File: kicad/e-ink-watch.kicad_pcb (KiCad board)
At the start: 4 copper layers, 40 x 40 mm, 42 parts, among them SW1 BTN1, SW2 BTN2, SW3 BTN3, U1 MDBT50Q-1MV2, U2 BQ25120A

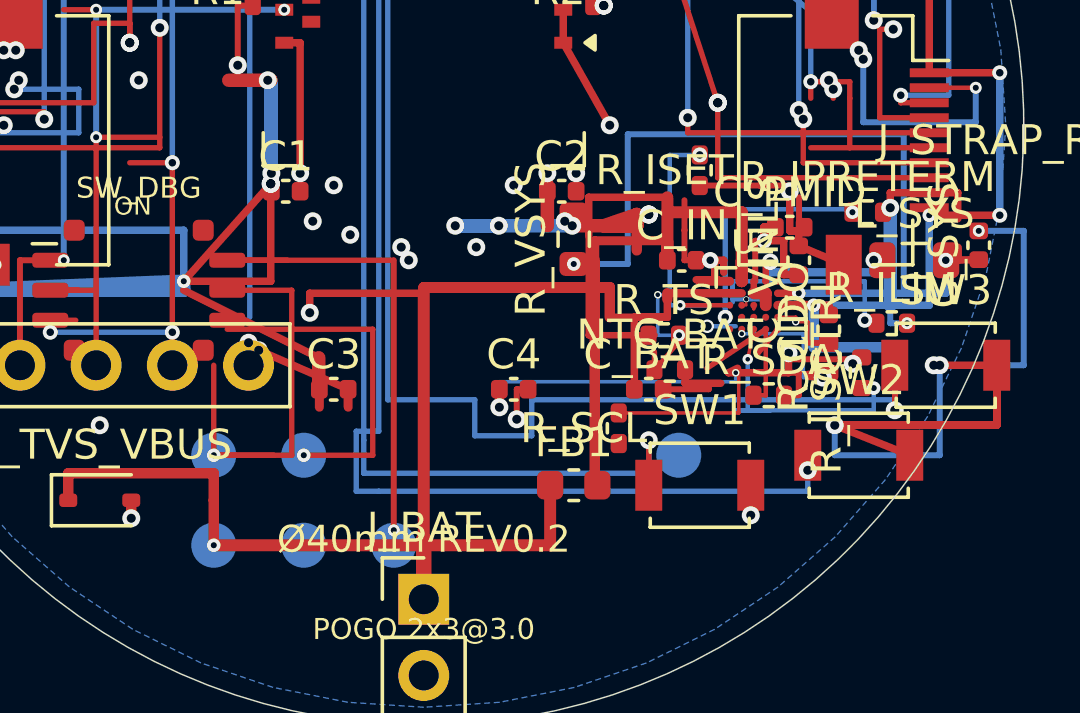
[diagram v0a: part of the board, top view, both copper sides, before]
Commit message: Pass-AT/AV: R_SCL on E5 (unc 6); VBUS jog cannot open I2C (#6)
* Pass-AL: keep the west GND via after a local In2 notch.

A 0.25/0.15 GND via on the west F end at (108.71, 108.15) joins the B.Cu pour. The In2 3V3 outline is notched with a 0.45 mm arc so the drill does not hit the plane. DRC stays shorting 0 and unconnected drops 8 to 7. South passives and U2 were not moved.

Co-authored-by: illiapliukhin <illiapliukhin@users.noreply.github.com>

* Pass-AM: record that R_SDA cannot leave x=111.4.

A larger placement search found an SCL hop under the 3V3 rail once the R_SDA vertical is gone, and a clear R_SCL site on that run. No R_SDA park has a 0.15 mm retie to E4, so the board is unchanged. Unconnected stays 7 and shorting stays 0.

Co-authored-by: illiapliukhin <illiapliukhin@users.noreply.github.com>

* Pass-AN: record that larger R_SDA moves still cannot retie 3V3.

The SCL hop at x=111.35 sits 0.015 mm from the B GND pour, so it stays unapplied. Unconnected remains 7 and shorting remains 0.

Co-authored-by: illiapliukhin <illiapliukhin@users.noreply.github.com>

* Pass-AO: record blocked PMIC_INT, TS, 3V3_DISP, and A5 stitches.

No footprint moved and no copper was added. Unconnected remains 7 and shorting remains 0.

Co-authored-by: illiapliukhin <illiapliukhin@users.noreply.github.com>

* Pass-AP: revert U2 zone move that joins SCL but raises shorting.

R_SCL onto E5 drops unc 7 to 6 and DRC then reports SWDIO_POGO to 3V3. Rigid 1-2 mm island shifts overlap. Board stays at the Pass-AL file.

Co-authored-by: illiapliukhin <illiapliukhin@users.noreply.github.com>

* Pass-AQ: revert clean U2 re-fanout; R_SCL on E5 still raises SWDIO short.

Shrinking the local 3V3 via and sliding the D5 GND via stays at shorting 0 and unc 7. Seating R_SCL on E5 drops unc to 6 and raises SWDIO_POGO↔3V3. Full revert; board stays the Pass-AL KEEP.

Co-authored-by: illiapliukhin <illiapliukhin@users.noreply.github.com>

* Pass-AR: revert SW_DBG move; pad 6 still overlaps the 3V3 dia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
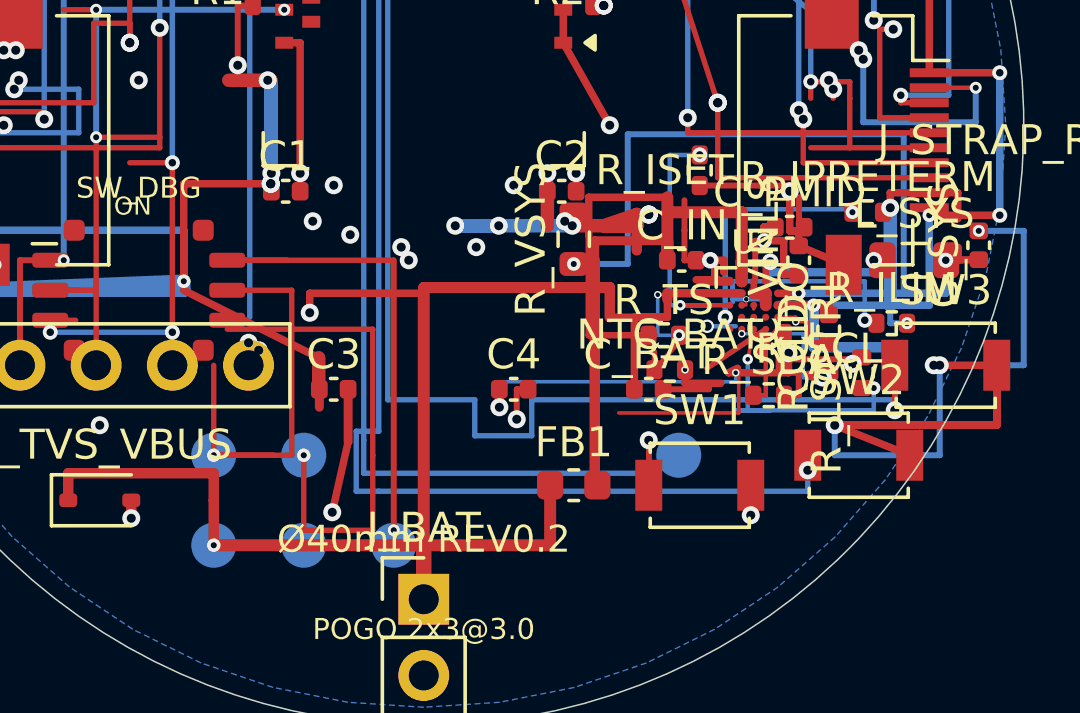
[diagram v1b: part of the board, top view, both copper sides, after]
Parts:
- moved R_SCL 6.11 mm to (112.0, 107.5), turned to 270 degrees
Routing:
- net nRESET_POGO: track 11.3 -> 16.3 mm
- net 3V3: track 114.8 -> 111.2 mm
- net GND: track 140.9 -> 141.2 mm, vias 44 -> 46
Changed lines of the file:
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@@
 	(footprint "Resistor_SMD:R_0402_1005Metric"
 		(layer "F.Cu")
-		(at 106.5 110.1 90)
+		(at 112 107.45 270)
 		(descr "Resistor SMD 0402 (1005 Metric), square (rectangular) end terminal, IPC-7351 nominal, (Body size source: IPC-SM-782 page 72, https://www.pcb-3d.com/wordpress/wp-content/uploads/ipc-sm-782a_amendment_1_and_2.pdf), generated with kicad-footprint-generator")
 		(tags "resistor")
@@
 	(segment
 		(start 97.48 108.8)
-		(end 97.48 109.399999)
+		(end 97.48 110.55)
 		(width 0.3)
 		(layer "F.Cu")
@@
 	)
 	(segment
-		(start 98.3 111)
-		(end 96 111)
-		(width 0.18)
-		(layer "F.Cu")
-		(net 25)
-	)
-	(segment
 		(start 98.3 106.8)
 		(end 98.3 111)
@@
 	)
 	(segment
-		(start 97.48 108.8)
-		(end 94.5 107.5)
-		(width 0.25)
-		(layer "F.Cu")
-		(net 1)
-	)
-	(segment
 		(start 85.0 96.5)
 		(end 85.0 94.5)
@@
 	(segment
 		(start 94.9 101.95)
-		(end 92.0 105.2)
+		(end 92.0 101.95)
 		(width 0.25)
 		(layer "F.Cu")
@@
 	)
 	(segment
-		(start 94.9 101.95)
-		(end 94.9 105.2)
+		(start 92.0 101.95)
+		(end 92.0 105.2)
 		(width 0.25)
 		(layer "F.Cu")
@@
 	)
 	(segment
-		(start 94.9 105.2)
+		(start 92.0 104.4)
 		(end 92.0 105.2)
 		(width 0.25)
@@
 	)
 	(via
+		(at 108.71 108.15)
+		(size 0.25)
+		(drill 0.15)
+		(layers "F.Cu" "B.Cu")
+		(net 1)
+	)
+	(segment
+		(start 97.48 110.55)
+		(end 96.95 112.9)
+		(width 0.25)
+		(layer "F.Cu")
+		(net 1)
+	)
+	(via
+		(at 96.95 112.9)
+		(size 0.6)
+		(drill 0.3)
+		(layers "F.Cu" "B.Cu")
+		(net 1)
+	)
+	(segment
+		(start 98.3 111)
+		(end 98.3 113.5)
+		(width 0.18)
+		(layer "F.Cu")
+		(net 25)
+	)
+	(segment
+		(start 98.3 113.5)
+		(end 96 113.5)
+		(width 0.18)
+		(layer "F.Cu")
+		(net 25)
+	)
+	(segment
+		(start 96 113.5)
+		(end 96 111)
+		(width 0.18)
+		(layer "F.Cu")
+		(net 25)
+	)
+	(via
